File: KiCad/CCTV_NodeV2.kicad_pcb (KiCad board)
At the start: 2 copper layers, 100 x 80 mm, 9 parts, among them J1 SOLAR, J2 BATT, U1 CN3791, U2 BMS 1S, U3 MT3608, U4 ESP32-S3, U5 OV7670

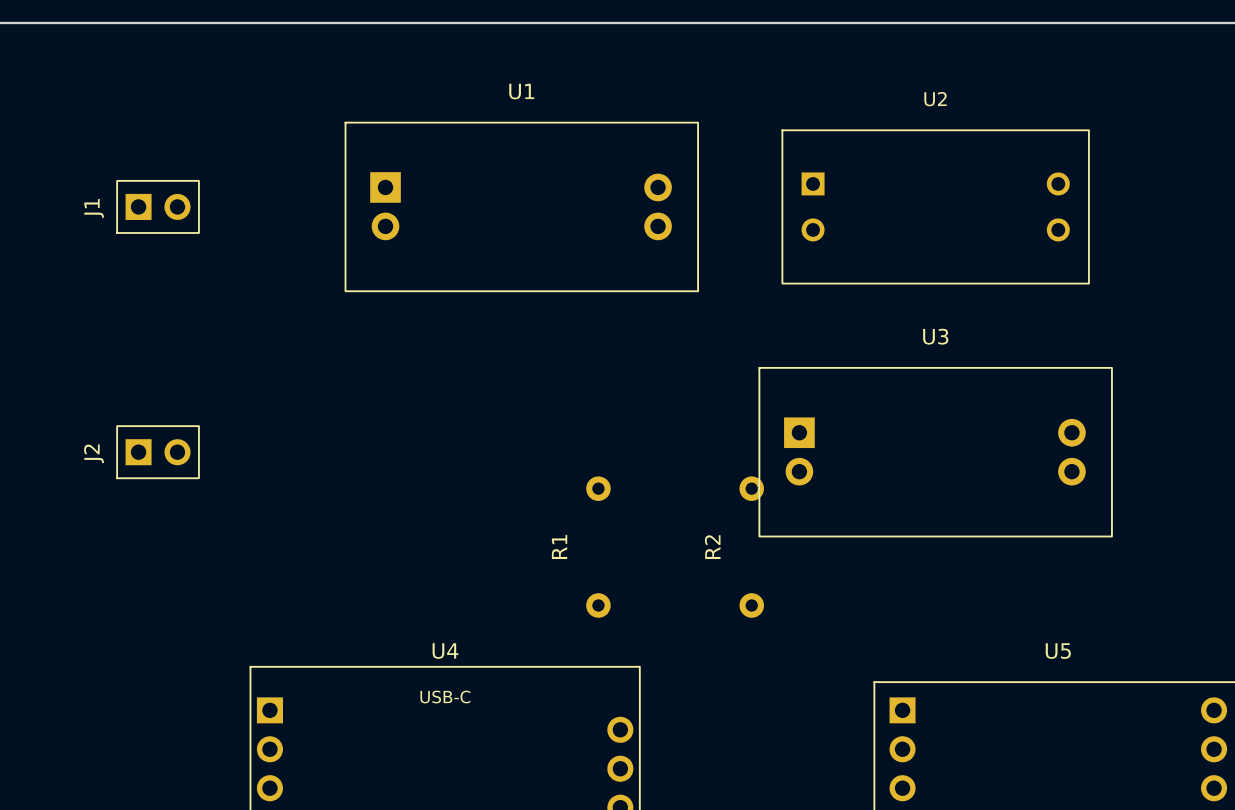
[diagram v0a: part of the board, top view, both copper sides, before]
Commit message: Route power nets at 1mm width on F.Cu
Adds 18 trace segments laid out on the front copper layer:

SOLAR+ (J1.1 -> U1.1)            : 1 segment diagonal
SOLAR- (J1.2 -> U1.2)            : 2 segments L-shape
BATT+  (U1.3, U2.1, U2.3 -> U3.1): 5 segments forming a top rail
                                    at y=5 with stubs down to each pad
BATT-  (U1.4 -> U2.2)            : 2 segments diagonal
+5V    (U3.3 -> U4.1)            : 4 segments around MT3608/U3 right
                                    edge, horizontal at y=40 under
                                    R1/R2, up to U4 5V pin
+3V3   (R1.1 -> R2.1 -> U5.1)    : 3 segments at y=38
GND    (U3.2 -> U3.4)            : 1 segment across MT3608 body

Still to route (left for user in pcbnew or Freerouting):
- J2.1/J2.2 -> BATT+/BATT- chain (left edge path needed)
- U4.3 -> R1.1 +3V3 (U4 right pad column blocks direct path)
- GND star network for U2.4, U4.2, U5.2, U5.4 (recommend a ground
  fill zone on B.Cu rather than discrete traces)
- All camera bus and data signals (14 nets)

Routing guide updated with status table showing which power nets are
done and which still need attention.
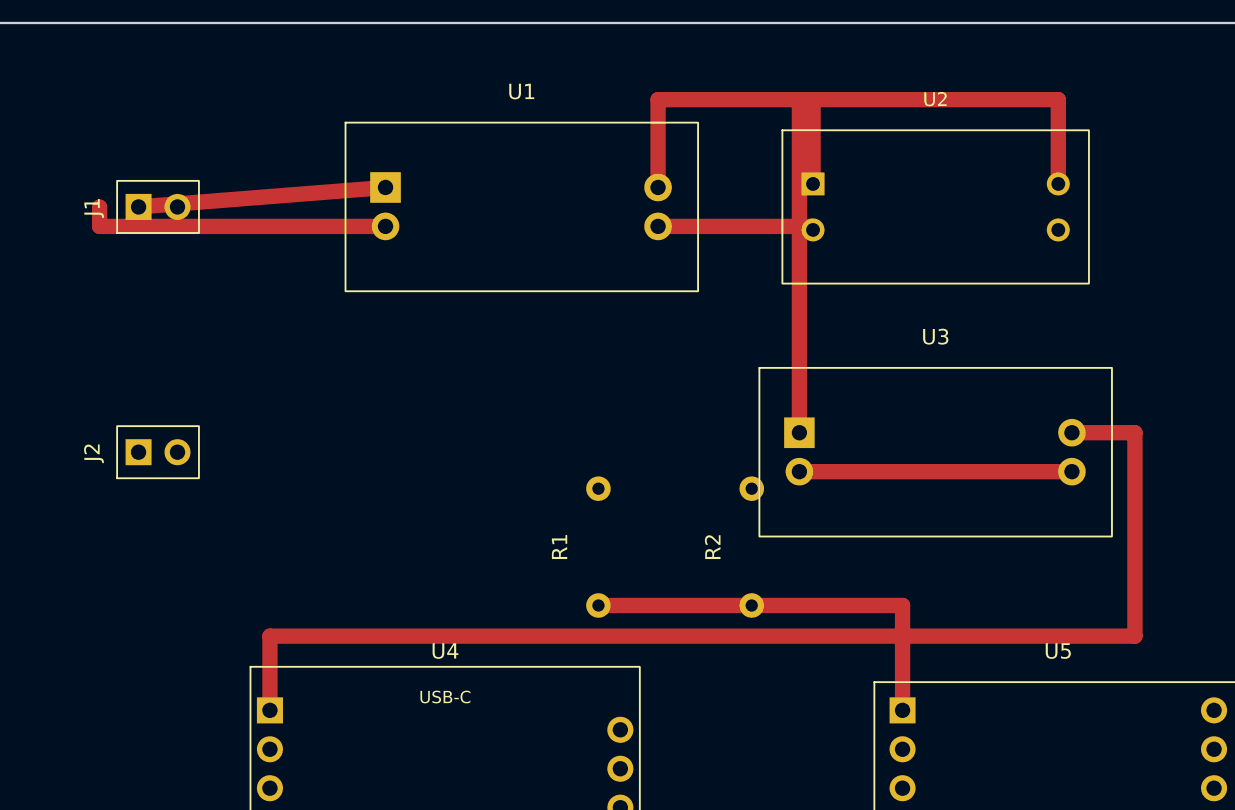
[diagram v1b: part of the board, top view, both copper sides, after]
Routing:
- net +5V: track 0.00 -> 78.7 mm
- net BATT+: track 0.00 -> 64.6 mm
- net +3V3: track 0.00 -> 26.7 mm
- net SOLAR-: track 0.00 -> 19.9 mm
- net GND: track 0.00 -> 17.8 mm
- net SOLAR+: track 0.00 -> 16.2 mm
- net BATT-: track 0.00 -> 10.3 mm
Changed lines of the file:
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@@
 		(pad "18" thru_hole circle (at 10.16 10.16) (size 1.7 1.7) (drill 1.0) (layers "*.Cu" "*.Mask") (net 14 "CAM_D0") (uuid "fp000009-p018-0000-0000-000000000009"))
 	)
+	(segment (start 10 12) (end 26.11 10.73) (width 1) (layer "F.Cu") (net 1) (uuid "trace0001-0000-0000-0000-000000000001"))
+	(segment (start 7.46 12) (end 7.46 13.27) (width 1) (layer "F.Cu") (net 2) (uuid "trace0002-0000-0000-0000-000000000002"))
+	(segment (start 7.46 13.27) (end 26.11 13.27) (width 1) (layer "F.Cu") (net 2) (uuid "trace0003-0000-0000-0000-000000000003"))
+	(segment (start 43.89 10.73) (end 43.89 5) (width 1) (layer "F.Cu") (net 3) (uuid "trace0004-0000-0000-0000-000000000004"))
+	(segment (start 43.89 5) (end 70 5) (width 1) (layer "F.Cu") (net 3) (uuid "trace0005-0000-0000-0000-000000000005"))
+	(segment (start 54 5) (end 54 10.5) (width 1) (layer "F.Cu") (net 3) (uuid "trace0006-0000-0000-0000-000000000006"))
+	(segment (start 70 5) (end 70 10.5) (width 1) (layer "F.Cu") (net 3) (uuid "trace0007-0000-0000-0000-000000000007"))
+	(segment (start 53.11 5) (end 53.11 26.73) (width 1) (layer "F.Cu") (net 3) (uuid "trace0008-0000-0000-0000-000000000008"))
+	(segment (start 43.89 13.27) (end 54 13.27) (width 1) (layer "F.Cu") (net 4) (uuid "trace0009-0000-0000-0000-000000000009"))
+	(segment (start 54 13.27) (end 54 13.5) (width 1) (layer "F.Cu") (net 4) (uuid "trace000a-0000-0000-0000-00000000000a"))
+	(segment (start 70.89 26.73) (end 75 26.73) (width 1) (layer "F.Cu") (net 6) (uuid "trace000b-0000-0000-0000-00000000000b"))
+	(segment (start 75 26.73) (end 75 40) (width 1) (layer "F.Cu") (net 6) (uuid "trace000c-0000-0000-0000-00000000000c"))
+	(segment (start 75 40) (end 18.57 40) (width 1) (layer "F.Cu") (net 6) (uuid "trace000d-0000-0000-0000-00000000000d"))
+	(segment (start 18.57 40) (end 18.57 44.84) (width 1) (layer "F.Cu") (net 6) (uuid "trace000e-0000-0000-0000-00000000000e"))
+	(segment (start 53.11 29.27) (end 70.89 29.27) (width 1) (layer "F.Cu") (net 5) (uuid "trace000f-0000-0000-0000-00000000000f"))
+	(segment (start 40 38) (end 50 38) (width 1) (layer "F.Cu") (net 7) (uuid "trace0010-0000-0000-0000-000000000010"))
+	(segment (start 50 38) (end 59.84 38) (width 1) (layer "F.Cu") (net 7) (uuid "trace0011-0000-0000-0000-000000000011"))
+	(segment (start 59.84 38) (end 59.84 44.84) (width 1) (layer "F.Cu") (net 7) (uuid "trace0012-0000-0000-0000-000000000012"))
 	(embedded_fonts no)
 )

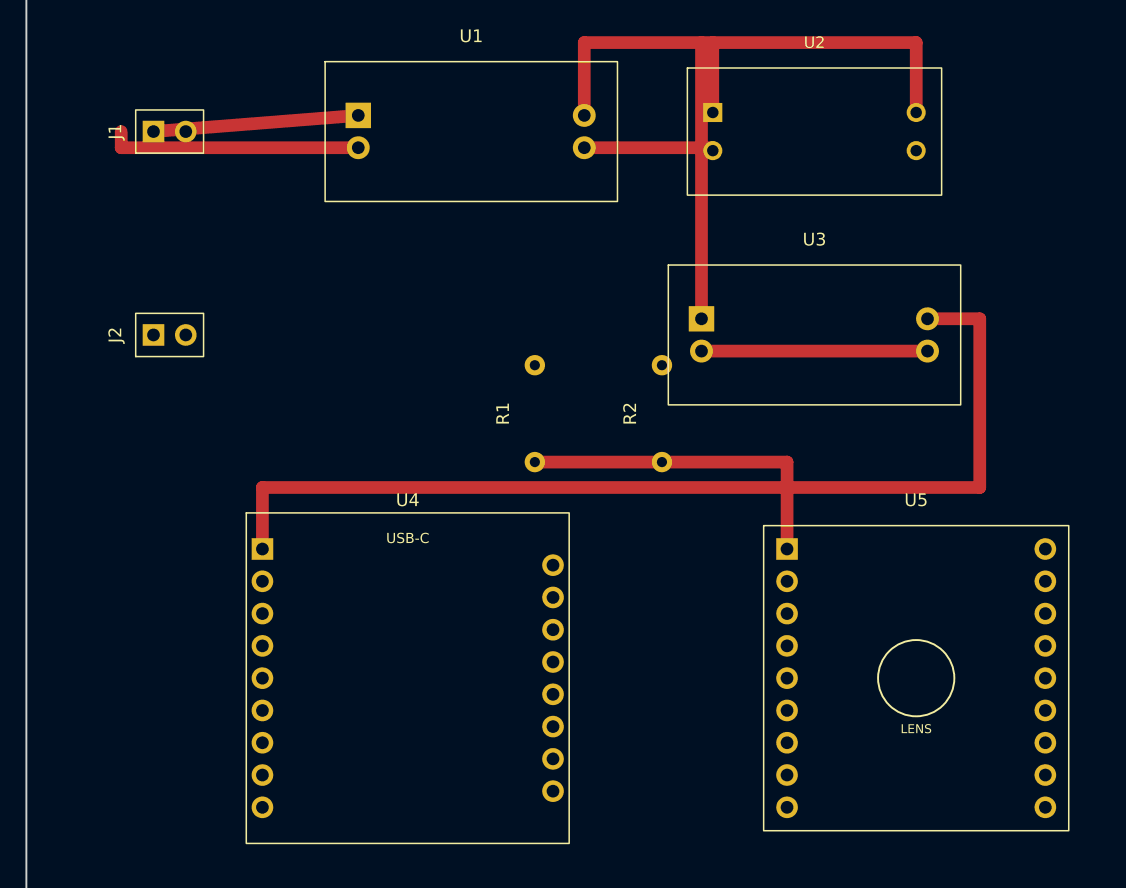
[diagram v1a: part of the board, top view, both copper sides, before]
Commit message: Route remaining signal + auxiliary power nets at 0.7mm
Adds 38 trace segments to CCTV_NodeV2.kicad_pcb:

Camera control on F.Cu (17 segments):
  SIOC : direct horizontal at y=55
  SIOD, VSYNC, HREF, PCLK : L-shape through inter-column gap
  XCLK : long path U4 left bottom -> over top of board -> U5 right

J2 connections on B.Cu (8 segments):
  J2.1 -> BATT+ : left edge at x=4, across y=8 above J1
  J2.2 -> BATT- : left edge at x=2, across y=16 below CN3791 top

U4.3 -> R1.1 +3V3 (3 segments F.Cu):
  exit U4.3 east through inter-column gap, north around R1, into R1.1

GND chain (10 segments F.Cu):
  U2.4 -> right edge -> U3.4
  U3.4 -> down through OV7670 body -> U5.2
  U5.2 -> bypass around U5.3 NC pad -> U5.4
  U4.2 -> horizontal at y=47.38 -> U5.2

Skipped: camera data bus (CAM_D0..D7, 8 nets). Reversed pin order
(U4 top=D0 / U5 bottom=D0) requires a twist pattern with vias that
Freerouting handles much better than hand-routing.

DRC note: many traces thread between 1.7mm header pads at 2.54mm
pitch, giving ~0.07mm trace-to-pad clearance vs KiCad's default
0.2mm. Either reduce clearance to 0.1mm in Board Setup, or narrow
the affected traces to 0.5mm. Both options documented in the
routing guide.
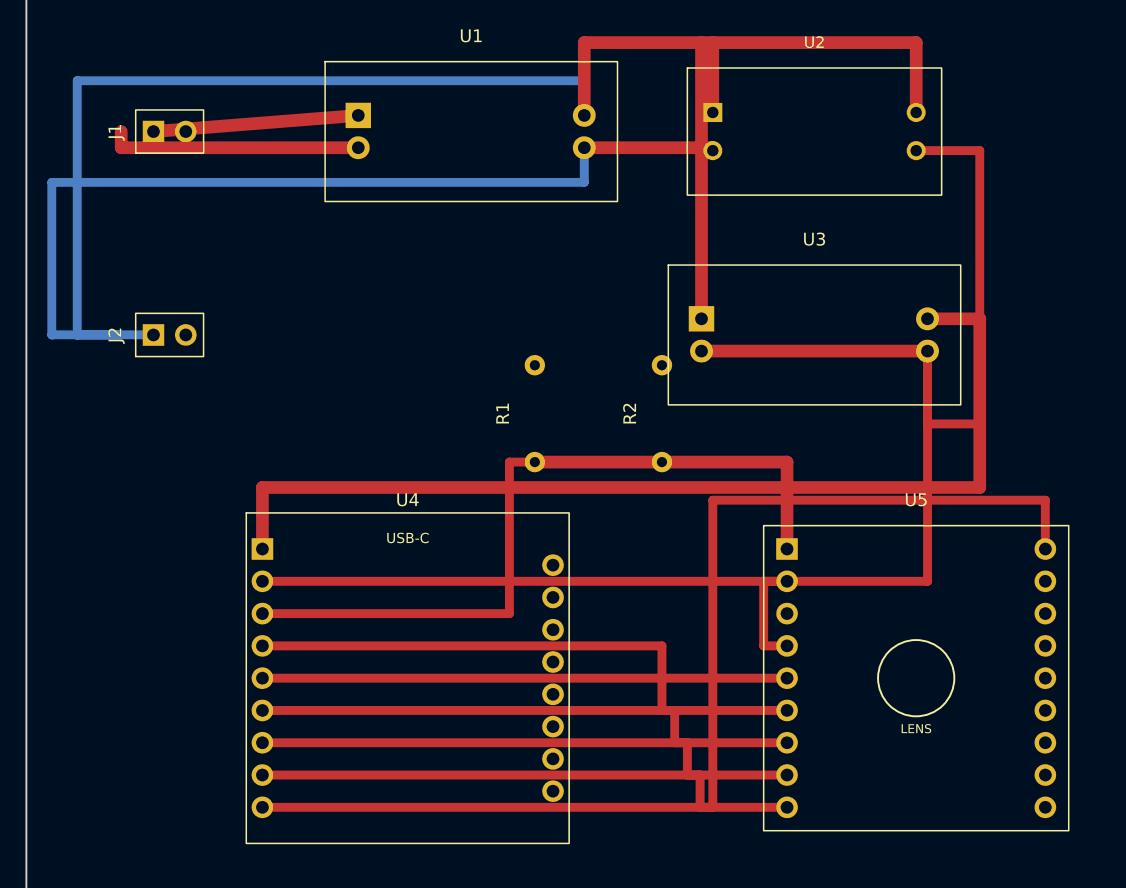
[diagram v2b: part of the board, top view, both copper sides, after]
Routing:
- net GND: track 17.8 -> 133.3 mm
- net XCLK: track 0.00 -> 89.6 mm
- net BATT+: track 64.6 -> 133.2 mm
- net BATT-: track 10.3 -> 72.4 mm
- net SIOD: track 0.00 -> 46.4 mm
- net VSYNC: track 0.00 -> 43.8 mm
- net PCLK: track 0.00 -> 43.8 mm
- net HREF: track 0.00 -> 43.8 mm
- net SIOC: track 0.00 -> 41.3 mm
- net +3V3: track 26.7 -> 60.0 mm
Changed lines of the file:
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@@
 	(segment (start 50 38) (end 59.84 38) (width 1) (layer "F.Cu") (net 7) (uuid "trace0011-0000-0000-0000-000000000011"))
 	(segment (start 59.84 38) (end 59.84 44.84) (width 1) (layer "F.Cu") (net 7) (uuid "trace0012-0000-0000-0000-000000000012"))
+	(segment (start 18.57 55) (end 59.84 55) (width 0.7) (layer "F.Cu") (net 9) (uuid "trace0013-0000-0000-0000-000000000013"))
+	(segment (start 18.57 52.46) (end 50 52.46) (width 0.7) (layer "F.Cu") (net 8) (uuid "trace0014-0000-0000-0000-000000000014"))
+	(segment (start 50 52.46) (end 50 57.54) (width 0.7) (layer "F.Cu") (net 8) (uuid "trace0015-0000-0000-0000-000000000015"))
+	(segment (start 50 57.54) (end 59.84 57.54) (width 0.7) (layer "F.Cu") (net 8) (uuid "trace0016-0000-0000-0000-000000000016"))
+	(segment (start 18.57 57.54) (end 51 57.54) (width 0.7) (layer "F.Cu") (net 10) (uuid "trace0017-0000-0000-0000-000000000017"))
+	(segment (start 51 57.54) (end 51 60.08) (width 0.7) (layer "F.Cu") (net 10) (uuid "trace0018-0000-0000-0000-000000000018"))
+	(segment (start 51 60.08) (end 59.84 60.08) (width 0.7) (layer "F.Cu") (net 10) (uuid "trace0019-0000-0000-0000-000000000019"))
+	(segment (start 18.57 60.08) (end 52 60.08) (width 0.7) (layer "F.Cu") (net 11) (uuid "trace001a-0000-0000-0000-00000000001a"))
+	(segment (start 52 60.08) (end 52 62.62) (width 0.7) (layer "F.Cu") (net 11) (uuid "trace001b-0000-0000-0000-00000000001b"))
+	(segment (start 52 62.62) (end 59.84 62.62) (width 0.7) (layer "F.Cu") (net 11) (uuid "trace001c-0000-0000-0000-00000000001c"))
+	(segment (start 18.57 62.62) (end 53 62.62) (width 0.7) (layer "F.Cu") (net 12) (uuid "trace001d-0000-0000-0000-00000000001d"))
+	(segment (start 53 62.62) (end 53 65.16) (width 0.7) (layer "F.Cu") (net 12) (uuid "trace001e-0000-0000-0000-00000000001e"))
+	(segment (start 53 65.16) (end 59.84 65.16) (width 0.7) (layer "F.Cu") (net 12) (uuid "trace001f-0000-0000-0000-00000000001f"))
+	(segment (start 18.57 65.16) (end 54 65.16) (width 0.7) (layer "F.Cu") (net 13) (uuid "trace0020-0000-0000-0000-000000000020"))
+	(segment (start 54 65.16) (end 54 41) (width 0.7) (layer "F.Cu") (net 13) (uuid "trace0021-0000-0000-0000-000000000021"))
+	(segment (start 54 41) (end 80.16 41) (width 0.7) (layer "F.Cu") (net 13) (uuid "trace0022-0000-0000-0000-000000000022"))
+	(segment (start 80.16 41) (end 80.16 44.84) (width 0.7) (layer "F.Cu") (net 13) (uuid "trace0023-0000-0000-0000-000000000023"))
+	(segment (start 10 28) (end 4 28) (width 0.7) (layer "B.Cu") (net 3) (uuid "trace0024-0000-0000-0000-000000000024"))
+	(segment (start 4 28) (end 4 8) (width 0.7) (layer "B.Cu") (net 3) (uuid "trace0025-0000-0000-0000-000000000025"))
+	(segment (start 4 8) (end 43.89 8) (width 0.7) (layer "B.Cu") (net 3) (uuid "trace0026-0000-0000-0000-000000000026"))
+	(segment (start 43.89 8) (end 43.89 10.73) (width 0.7) (layer "B.Cu") (net 3) (uuid "trace0027-0000-0000-0000-000000000027"))
+	(segment (start 7.46 28) (end 2 28) (width 0.7) (layer "B.Cu") (net 4) (uuid "trace0028-0000-0000-0000-000000000028"))
+	(segment (start 2 28) (end 2 16) (width 0.7) (layer "B.Cu") (net 4) (uuid "trace0029-0000-0000-0000-000000000029"))
+	(segment (start 2 16) (end 43.89 16) (width 0.7) (layer "B.Cu") (net 4) (uuid "trace002a-0000-0000-0000-00000000002a"))
+	(segment (start 43.89 16) (end 43.89 13.27) (width 0.7) (layer "B.Cu") (net 4) (uuid "trace002b-0000-0000-0000-00000000002b"))
+	(segment (start 18.57 49.92) (end 38 49.92) (width 0.7) (layer "F.Cu") (net 7) (uuid "trace002c-0000-0000-0000-00000000002c"))
+	(segment (start 38 49.92) (end 38 38) (width 0.7) (layer "F.Cu") (net 7) (uuid "trace002d-0000-0000-0000-00000000002d"))
+	(segment (start 38 38) (end 40 38) (width 0.7) (layer "F.Cu") (net 7) (uuid "trace002e-0000-0000-0000-00000000002e"))
+	(segment (start 70 13.5) (end 75 13.5) (width 0.7) (layer "F.Cu") (net 5) (uuid "trace002f-0000-0000-0000-00000000002f"))
+	(segment (start 75 13.5) (end 75 35) (width 0.7) (layer "F.Cu") (net 5) (uuid "trace0030-0000-0000-0000-000000000030"))
+	(segment (start 75 35) (end 70.89 35) (width 0.7) (layer "F.Cu") (net 5) (uuid "trace0031-0000-0000-0000-000000000031"))
+	(segment (start 70.89 35) (end 70.89 29.27) (width 0.7) (layer "F.Cu") (net 5) (uuid "trace0032-0000-0000-0000-000000000032"))
+	(segment (start 70.89 29.27) (end 70.89 47.38) (width 0.7) (layer "F.Cu") (net 5) (uuid "trace0033-0000-0000-0000-000000000033"))
+	(segment (start 70.89 47.38) (end 59.84 47.38) (width 0.7) (layer "F.Cu") (net 5) (uuid "trace0034-0000-0000-0000-000000000034"))
+	(segment (start 59.84 47.38) (end 58 47.38) (width 0.7) (layer "F.Cu") (net 5) (uuid "trace0035-0000-0000-0000-000000000035"))
+	(segment (start 58 47.38) (end 58 52.46) (width 0.7) (layer "F.Cu") (net 5) (uuid "trace0036-0000-0000-0000-000000000036"))
+	(segment (start 58 52.46) (end 59.84 52.46) (width 0.7) (layer "F.Cu") (net 5) (uuid "trace0037-0000-0000-0000-000000000037"))
+	(segment (start 18.57 47.38) (end 59.84 47.38) (width 0.7) (layer "F.Cu") (net 5) (uuid "trace0038-0000-0000-0000-000000000038"))
 	(embedded_fonts no)
 )
